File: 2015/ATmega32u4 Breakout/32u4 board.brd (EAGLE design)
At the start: 21.2 x 40.8 mm, 21 parts, among them X1 MINI-USB-UX60A-MB-5ST

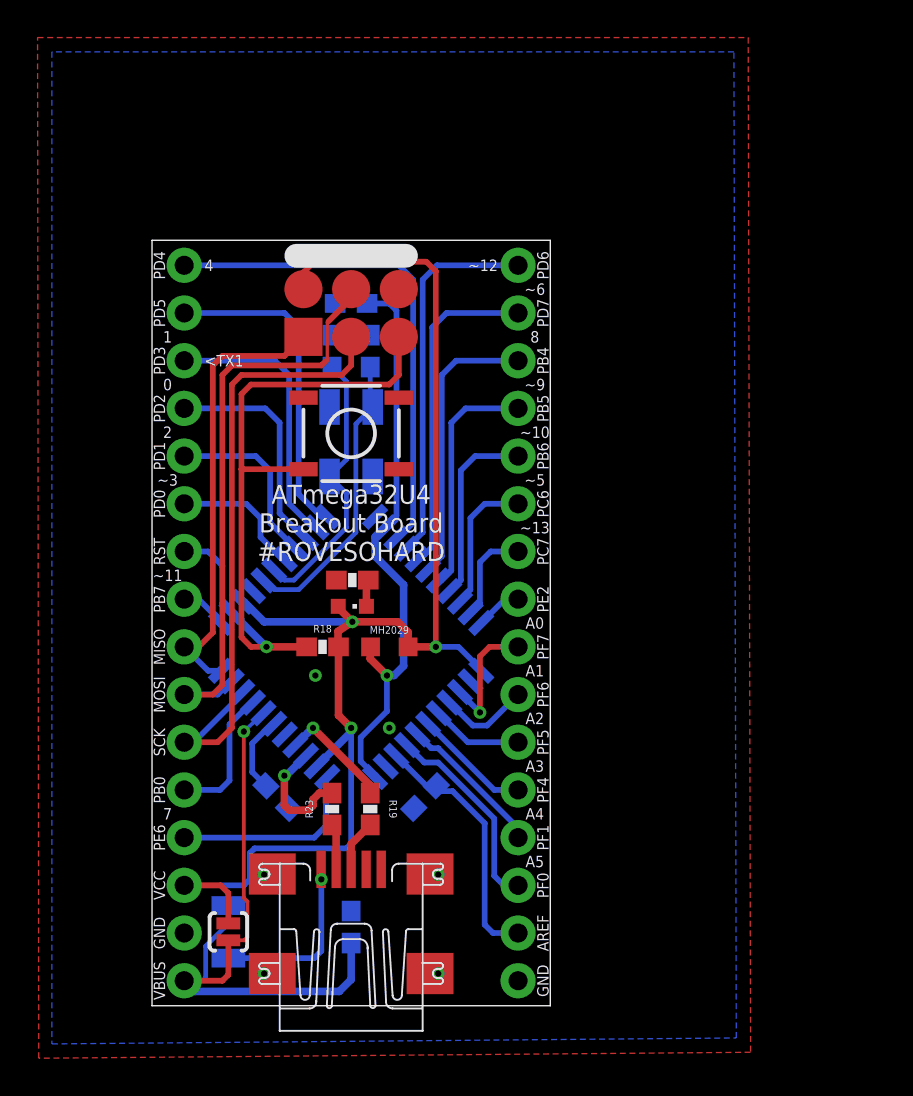
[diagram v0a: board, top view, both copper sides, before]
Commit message: Started adding Castellated Edges
http://lmgtfy.com/?q=Castellated+Edges
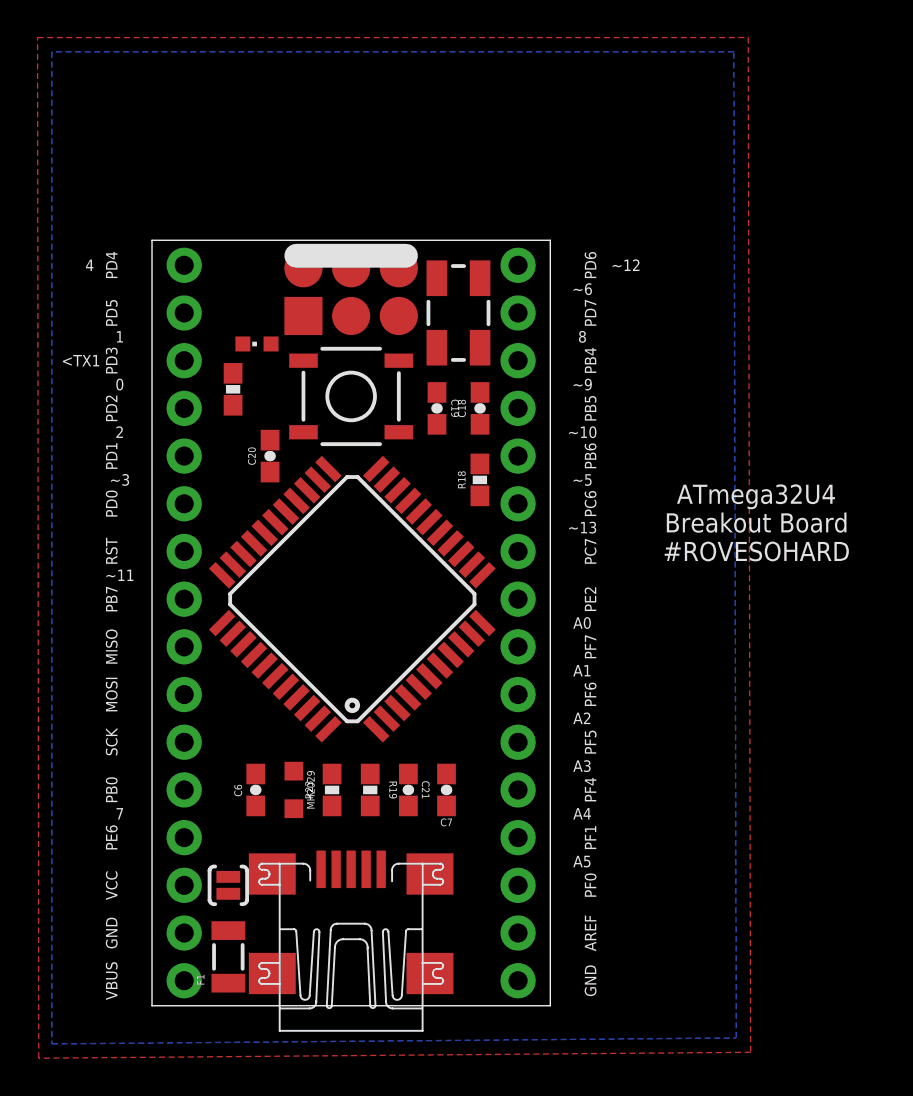
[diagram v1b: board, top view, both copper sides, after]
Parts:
- moved LED1 14.9 mm to (5.59, 35.2), turned to 90 degrees
- moved R18 12.2 mm to (17.5, 28.0), turned to 90 degrees
- moved R1 12.0 mm to (4.32, 32.8), turned to 90 degrees
- moved C20 9.20 mm to (6.29, 29.3), flipped to the top, turned to 90 degrees
- moved MH2029 9.16 mm to (7.56, 11.5), turned to 270 degrees
- moved U$4 8.93 mm to (16.3, 36.9), flipped to the top, turned to 90 degrees
- moved C7 8.90 mm to (15.7, 11.5), flipped to the top, turned to 270 degrees
- moved C18 6.60 mm to (17.5, 31.8), flipped to the top
- moved C19 6.37 mm to (15.2, 31.8), flipped to the top
- moved U$3 2.54 mm to (10.7, 21.7), flipped to the top
- moved SJ1 2.48 mm to (4.06, 6.41)
- moved S1 1.97 mm to (10.6, 32.4)
- moved F1 1.33 mm to (4.06, 2.60), flipped to the top, turned to 90 degrees
- moved C6 1.20 mm to (5.52, 11.5), flipped to the top, turned to 90 degrees
- moved U$2 1.11 mm to (10.6, 38.0)
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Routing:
- net VCC: track 74.4 -> 0.00 mm, vias 3 -> 0
- net RST: track 38.4 -> 0.00 mm, vias 1 -> 0
- net VBUS: track 34.8 -> 0.00 mm, vias 1 -> 0
- net SCK: track 33.7 -> 0.00 mm
- net MOSI: track 31.9 -> 0.00 mm
- net N$31: track 31.1 -> 0.00 mm, vias 1 -> 0
- net PD4: track 26.7 -> 0.00 mm
- net MISO: track 24.0 -> 0.00 mm
- net PD6: track 20.1 -> 0.00 mm
- net PD7: track 17.6 -> 0.00 mm
- net PD5: track 17.3 -> 0.00 mm
- net N$41: track 15.9 -> 0.00 mm
- net PB4: track 15.1 -> 0.00 mm
- net N$39: track 14.8 -> 0.00 mm
- net PD3: track 14.7 -> 0.00 mm
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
